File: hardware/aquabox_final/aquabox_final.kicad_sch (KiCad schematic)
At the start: 0 parts

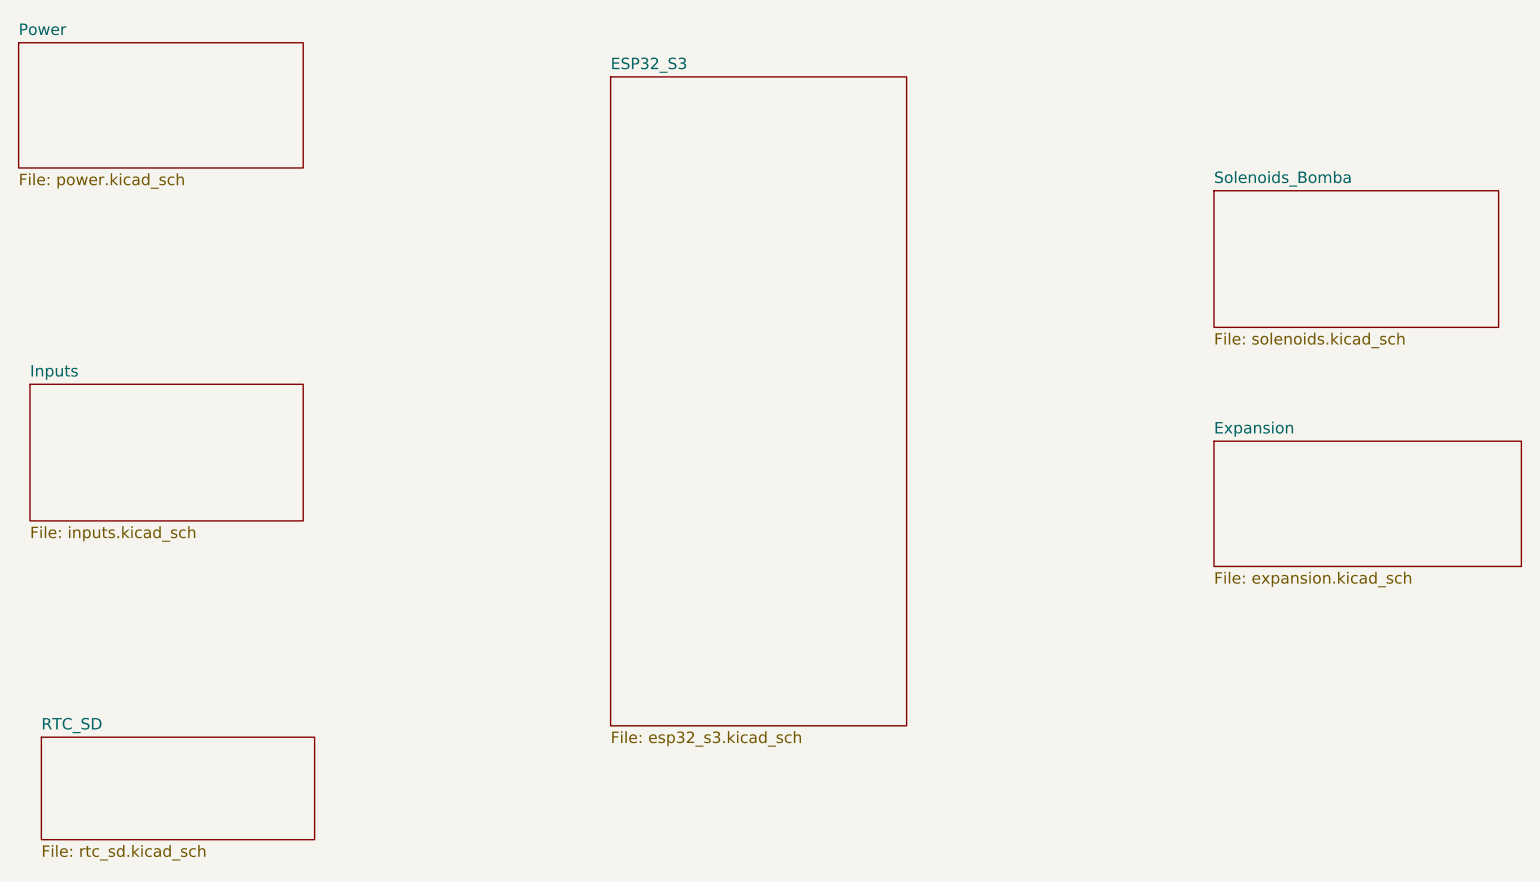
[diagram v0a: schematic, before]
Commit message: Implementação do RTC
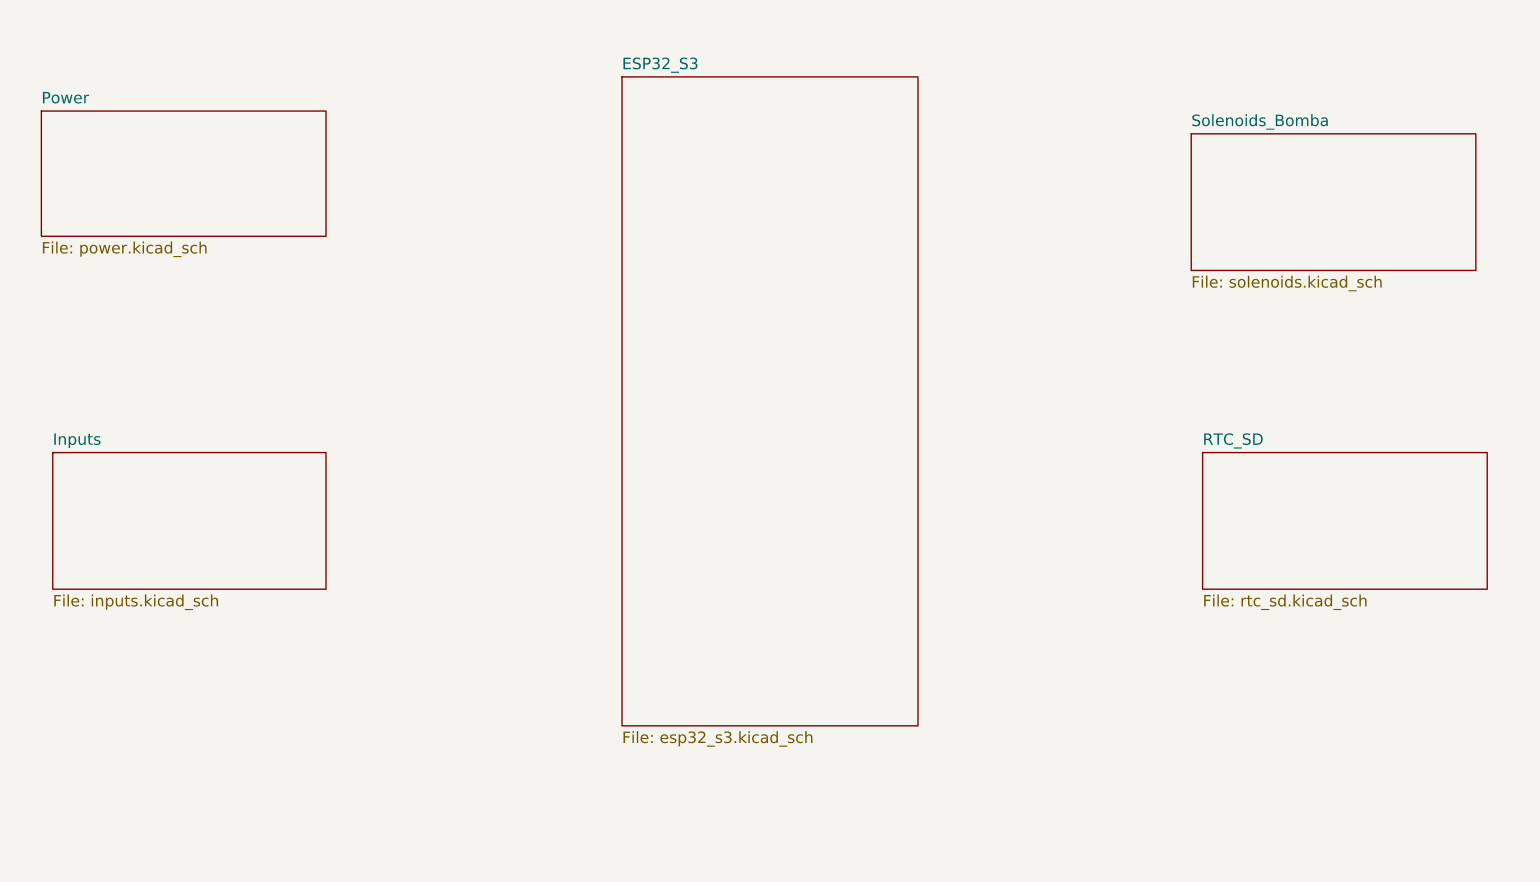
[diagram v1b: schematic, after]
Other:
- removed sheet Expansion
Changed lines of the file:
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@@
 	)
 	(sheet
-		(at 62.23 86.36)
+		(at 64.77 93.98)
 		(size 30.48 15.24)
 		(exclude_from_sim no)
@@
 		)
 		(property "Sheetname" "Inputs"
-			(at 62.23 85.6484 0)
+			(at 64.77 93.2684 0)
 			(show_name no)
 			(do_not_autoplace no)
@@
 		)
 		(property "Sheetfile" "inputs.kicad_sch"
-			(at 62.23 102.1846 0)
+			(at 64.77 109.8046 0)
 			(show_name no)
 			(do_not_autoplace no)
@@
 	)
 	(sheet
-		(at 63.5 125.73)
-		(size 30.48 11.43)
+		(at 193.04 93.98)
+		(size 31.75 15.24)
 		(exclude_from_sim no)
 		(in_bom yes)
@@
 		)
 		(property "Sheetname" "RTC_SD"
-			(at 63.5 125.0184 0)
+			(at 193.04 93.2684 0)
 			(show_name no)
 			(do_not_autoplace no)
@@
 		)
 		(property "Sheetfile" "rtc_sd.kicad_sch"
-			(at 63.5 137.7446 0)
+			(at 193.04 109.8046 0)
 			(show_name no)
 			(do_not_autoplace no)
@@
 	)
 	(sheet
-		(at 127 52.07)
+		(at 128.27 52.07)
 		(size 33.02 72.39)
 		(exclude_from_sim no)
@@
 		)
 		(property "Sheetname" "ESP32_S3"
-			(at 127 51.3584 0)
+			(at 128.27 51.3584 0)
 			(show_name no)
 			(do_not_autoplace no)
@@
 		)
 		(property "Sheetfile" "esp32_s3.kicad_sch"
-			(at 127 125.0446 0)
+			(at 128.27 125.0446 0)
 			(show_name no)
 			(do_not_autoplace no)
@@
 	)
 	(sheet
-		(at 60.96 48.26)
+		(at 63.5 55.88)
 		(size 31.75 13.97)
 		(exclude_from_sim no)
@@
 		)
 		(property "Sheetname" "Power"
-			(at 60.96 47.5484 0)
+			(at 63.5 55.1684 0)
 			(show_name no)
 			(do_not_autoplace no)
@@
 		)
 		(property "Sheetfile" "power.kicad_sch"
-			(at 60.96 62.8146 0)
+			(at 63.5 70.4346 0)
 			(show_name no)
 			(do_not_autoplace no)
@@
 	)
 	(sheet
-		(at 194.31 92.71)
-		(size 34.29 13.97)
-		(exclude_from_sim no)
-		(in_bom yes)
-		(on_board yes)
-		(dnp no)
-		(fields_autoplaced yes)
-		(stroke
-			(width 0.1524)
-			(type solid)
-		)
-		(fill
-			(color 0 0 0 0)
-		)
-		(property "Sheetname" "Expansion"
-			(at 194.31 91.9984 0)
-			(show_name no)
-			(do_not_autoplace no)
-			(effects
-				(font
-					(size 1.27 1.27)
-				)
-				(justify left bottom)
-			)
-		)
-		(property "Sheetfile" "expansion.kicad_sch"
-			(at 194.31 107.2646 0)
-			(show_name no)
-			(do_not_autoplace no)
-			(effects
-				(font
-					(size 1.27 1.27)
-				)
-				(justify left top)
-			)
-		)
-		(instances
-			(project "aquabox_final"
-				(path "/c895ac8d-c639-4fea-ba83-739985d9c75e"
-					(page "7")
-				)
-			)
-		)
-	)
-	(sheet
-		(at 194.31 64.77)
+		(at 191.77 58.42)
 		(size 31.75 15.24)
 		(exclude_from_sim no)
@@
 		)
 		(property "Sheetname" "Solenoids_Bomba"
-			(at 194.31 64.0584 0)
+			(at 191.77 57.7084 0)
 			(show_name no)
 			(do_not_autoplace no)
@@
 		)
 		(property "Sheetfile" "solenoids.kicad_sch"
-			(at 194.31 80.5946 0)
-			(show_name no)
-			(do_not_autoplace no)
+			(at 191.77 74.2446 0)
+			(show_name no)
+			(do_not_autoplace no)
